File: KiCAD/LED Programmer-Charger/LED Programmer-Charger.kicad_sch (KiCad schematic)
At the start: 17 parts, among them J1 USB_B_Micro, J2 UPDI socket, SW2 SW_SPDT, U1 CH340C, U2 LTC4126EV-10_TRMPBF

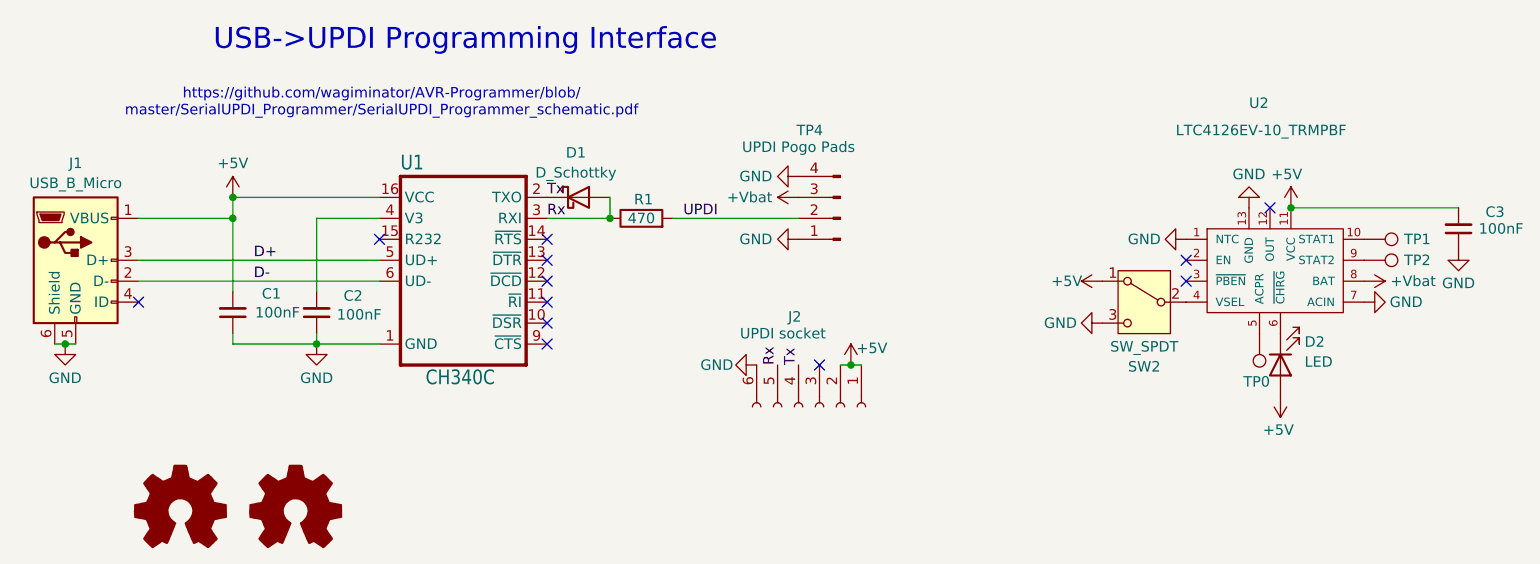
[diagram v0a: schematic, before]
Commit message: Remove status pads for charger as DC-DC converter is required
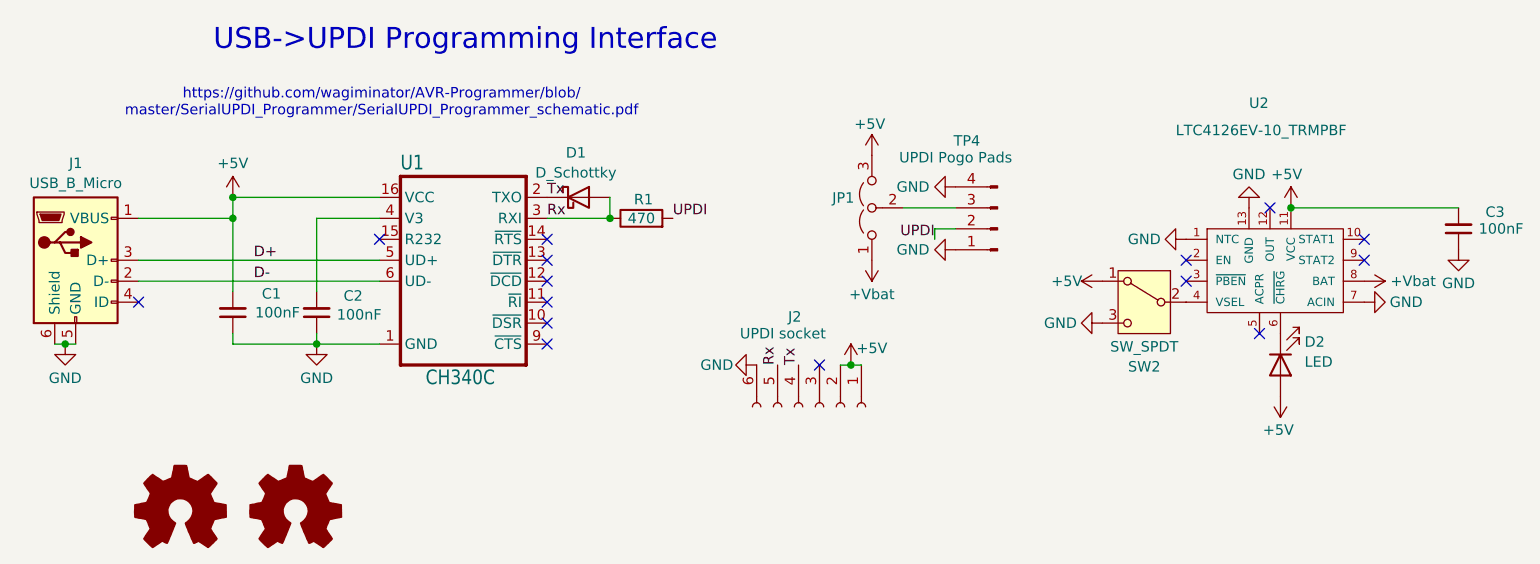
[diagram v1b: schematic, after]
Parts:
- removed TP0, TP1, TP2: TestPoint, TestPoint:TestPoint_Pad_D2.0mm, symbol Connector:TestPoint
- added JP1: Jumper_3_Open, Jumper:SolderJumper-3_P2.0mm_Open_TrianglePad1.0x1.5mm, symbol Jumper:Jumper_3_Open
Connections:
- net +5V: now also JP1.3 (B)
- net +Vbat: now also JP1.1 (A); no longer TP4.3 (Pin_3)
- new net: JP1.2 (C), TP4.3 (Pin_3)
- no-connect marks 12 -> 15
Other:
- moved on the sheet: TP4
